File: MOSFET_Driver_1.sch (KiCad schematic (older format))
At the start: 20 parts, among them Q1 TPHR8504PL, Q2 TPHR8504PL, Q3 TPHR8504PL, Q4 TPHR8504PL, Q5 TPHR8504PL, Q6 TPHR8504PL, U1 FD6288Q

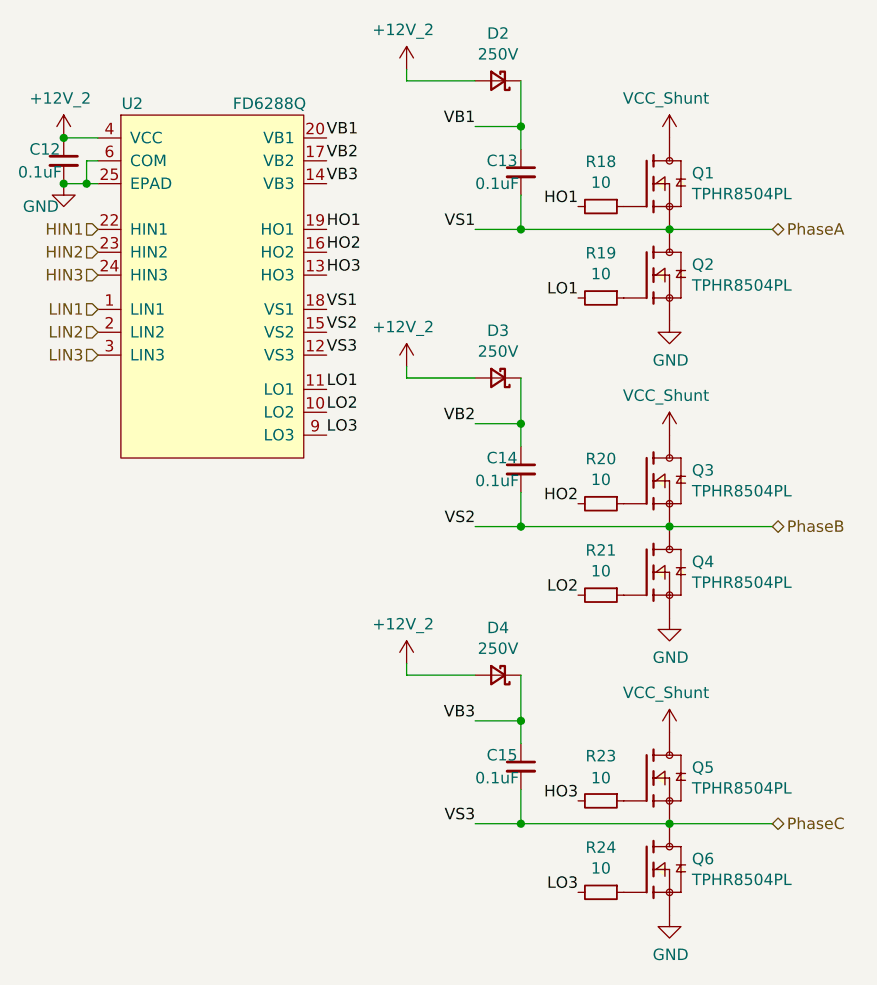
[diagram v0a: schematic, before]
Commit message: Lots of changes made with back being rerouted
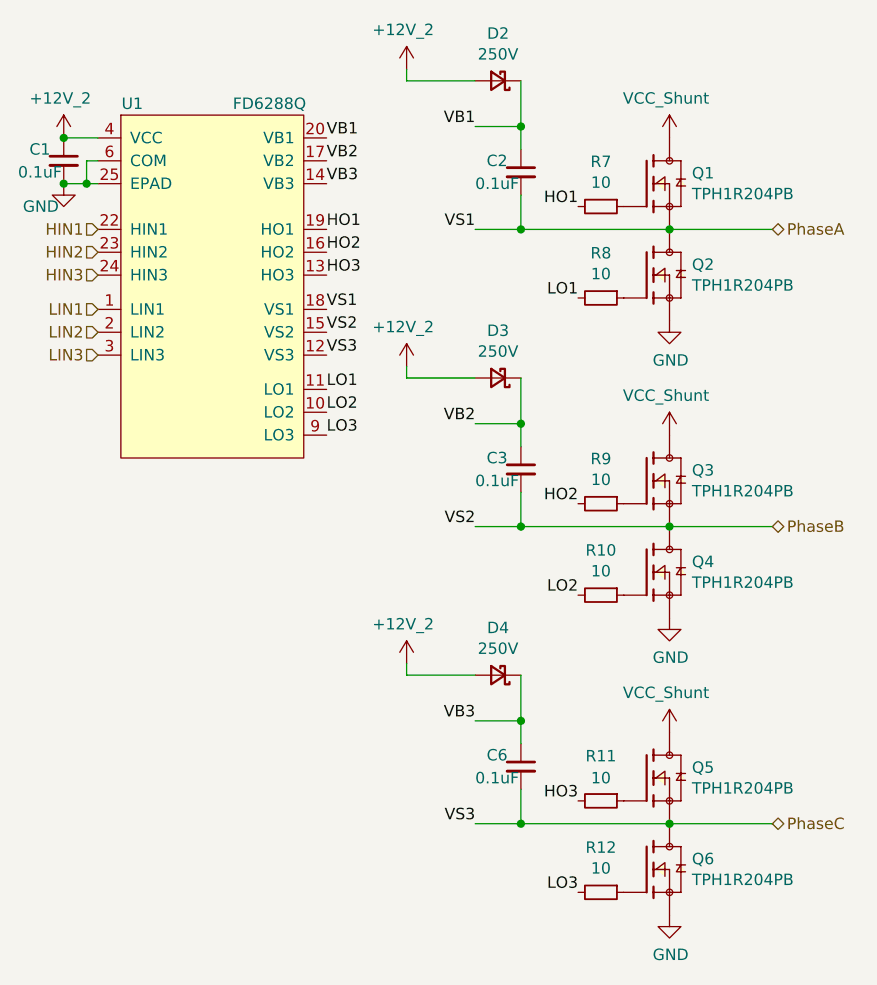
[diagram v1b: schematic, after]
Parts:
- removed Q1, Q2, Q3, Q4, Q5, Q6: TPHR8504PL, Footprints:TPHR8504PL, symbol JPW_Symbols:TPHR8504PL
- added Q1, Q2, Q3, Q4, Q5, Q6: TPH1R204PB, Footprints:TPH1R204PB, symbol JPW_Symbols:TPH1R204PB
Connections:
- net GND: now also Q2.1, Q2.2, Q2.3, Q4.1, Q4.2, Q4.3, Q6.1, Q6.2, Q6.3
- net PhaseA: now also Q1.1, Q1.2, Q1.3, Q2.5, Q2.6, Q2.7, Q2.8, Q2.9
- net PhaseB: now also Q3.1, Q3.2, Q3.3, Q4.5, Q4.6, Q4.7, Q4.8, Q4.9
- net PhaseC: now also Q5.1, Q5.2, Q5.3, Q6.5, Q6.6, Q6.7, Q6.8, Q6.9
- net VCC_Shunt: now also Q1.5, Q1.6, Q1.7, Q1.8, Q1.9, Q3.5, Q3.6, Q3.7, Q3.8, Q3.9, Q5.5, Q5.6, Q5.7, Q5.8, Q5.9
- net at R8.1: now also Q2.4
- net at R7.1: now also Q1.4
- net at R10.1: now also Q4.4
- net at R9.1: now also Q3.4
- net at R11.1: now also Q5.4
- net at R12.1: now also Q6.4

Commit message: Added stuff
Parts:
- C11: Notes (none) -> 12V Rated
- C12, C13, C14: Notes (none) -> VCC Rated
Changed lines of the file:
@@
 F 2 "Capacitor_SMD:C_0402_1005Metric" H 5500 2100 50  0001 C CNN
 F 3 "~" H 5500 2100 50  0001 C CNN
+F 4 "12V Rated" H 5500 2100 50  0001 C CNN "Notes"
 	1    5500 2100
 	1    0    0    -1
@@
 F 2 "Capacitor_SMD:C_0603_1608Metric" H 7500 3450 50  0001 C CNN
 F 3 "~" H 7500 3450 50  0001 C CNN
+F 4 "VCC Rated" H 7500 3450 50  0001 C CNN "Notes"
 	1    7500 3450
 	1    0    0    -1
@@
 F 2 "Capacitor_SMD:C_0603_1608Metric" H 7500 2150 50  0001 C CNN
 F 3 "~" H 7500 2150 50  0001 C CNN
+F 4 "VCC Rated" H 7500 2150 50  0001 C CNN "Notes"
 	1    7500 2150
 	1    0    0    -1
@@
 F 2 "Capacitor_SMD:C_0603_1608Metric" H 7500 4750 50  0001 C CNN
 F 3 "~" H 7500 4750 50  0001 C CNN
+F 4 "VCC Rated" H 7500 4750 50  0001 C CNN "Notes"
 	1    7500 4750
 	1    0    0    -1
